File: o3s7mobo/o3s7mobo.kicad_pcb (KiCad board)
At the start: 2 copper layers, 330 x 217 mm, 43 parts, among them M1541 M1541, M1543 M1543

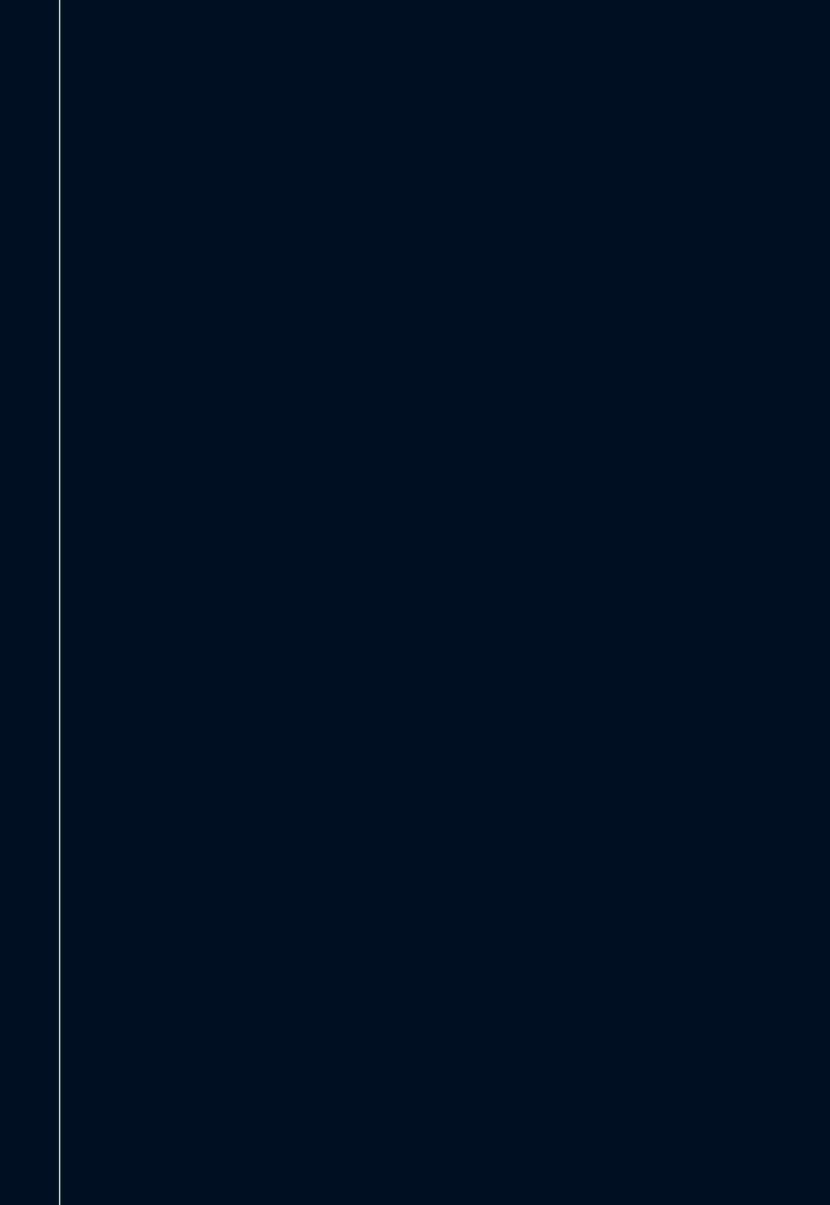
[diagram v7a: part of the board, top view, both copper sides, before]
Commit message: Added keyboard and mouse connectors
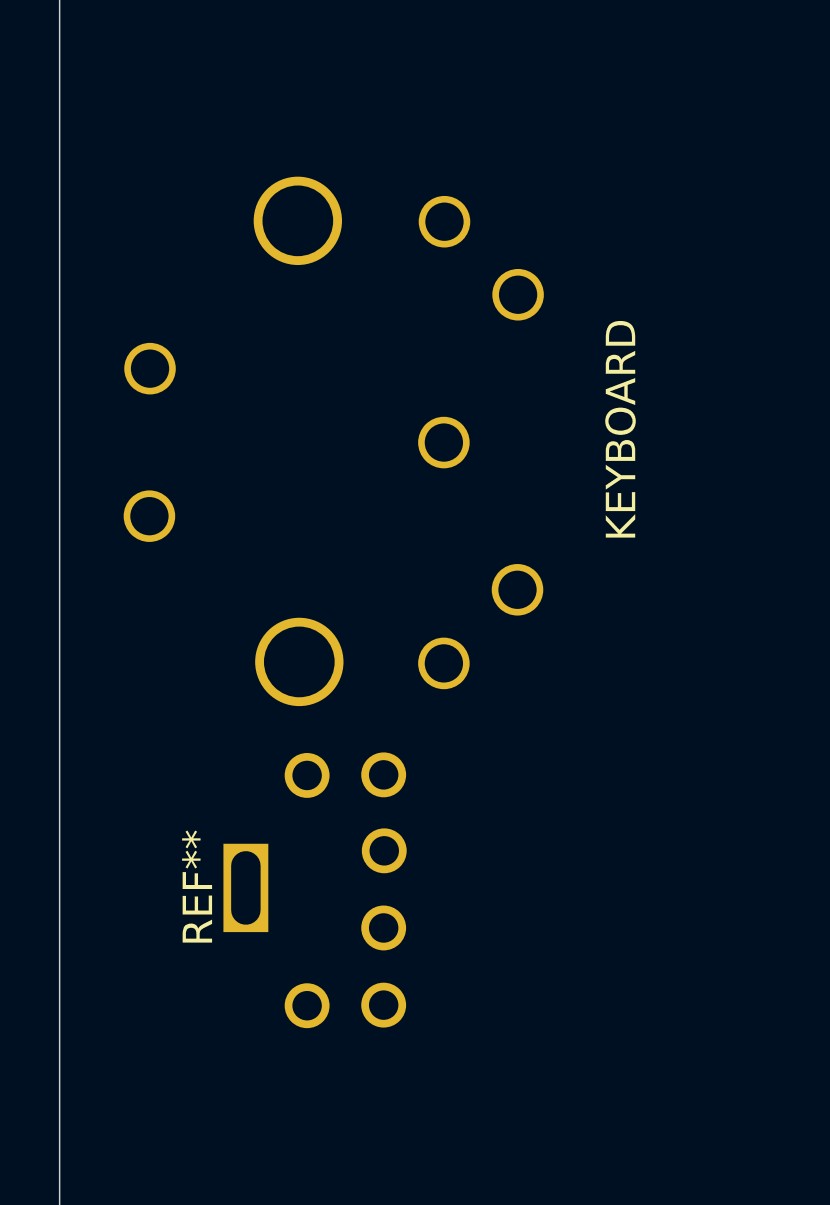
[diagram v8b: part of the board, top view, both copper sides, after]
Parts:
- added KEYBOARD: ATkeyboard, Downloaded:ATkeyboard, F.Cu at (18.6, 27.0)
- added REF**: PS2, Downloaded:PS2, F.Cu at (4.21, 42.1)
